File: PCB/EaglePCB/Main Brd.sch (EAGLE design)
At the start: 57 parts, among them J1 1909763-1, J3 1909763-1, U1 ATWINC1500-MR210PB1952-T, U3 MSP430FR2355TDBTRDBT0038A_M, U6 ARJM11C7-114-BA-EW2

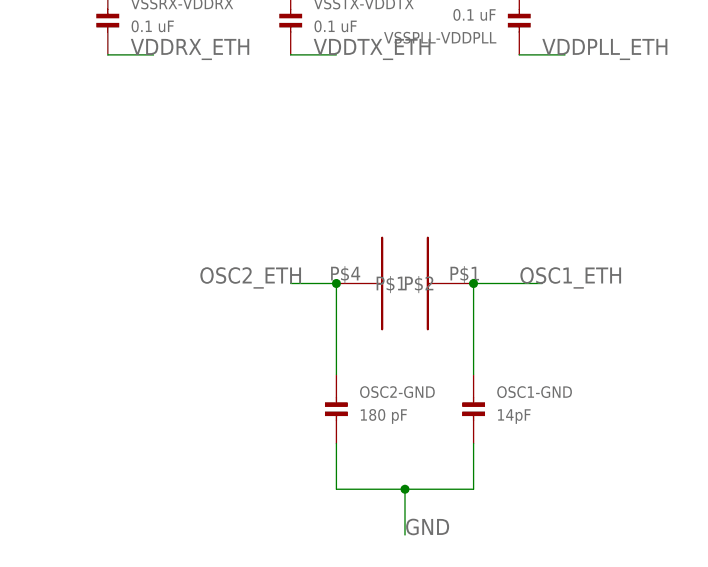
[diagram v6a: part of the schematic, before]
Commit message: new oscillator added into circuit
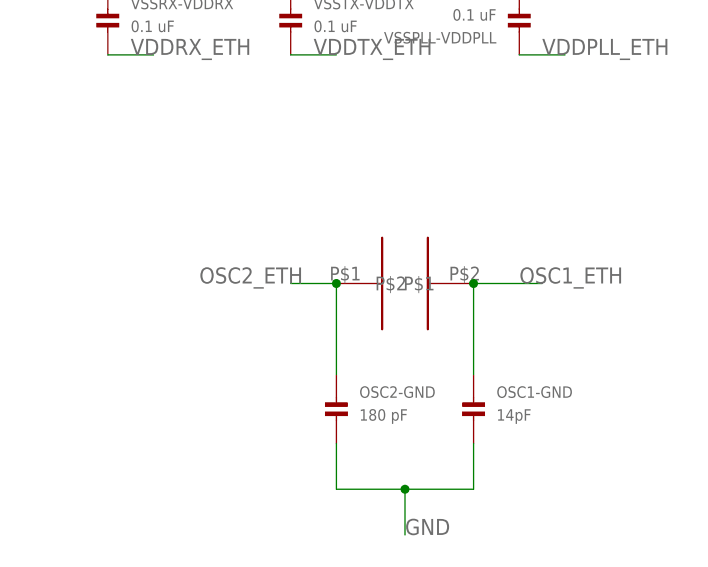
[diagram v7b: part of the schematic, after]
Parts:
- U$2: value CRYSTAL -> J49SMH-P-G-G-K-25M0; device 473:CRYSTAL -> 473:J49SMH-P-G-G-K-25M0
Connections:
- net OSC1_ETH: now also U$2.P$2; no longer U$2.P$1
- net OSC2_ETH: now also U$2.P$1; no longer U$2.P$2
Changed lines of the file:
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@@
 <grid distance="0.1" unitdist="inch" unit="inch" style="lines" multiple="1" display="no" altdistance="0.01" altunitdist="inch" altunit="inch"/>
 <layers>
-<layer number="1" name="Top" color="4" fill="1" visible="no" active="no"/>
-<layer number="16" name="Bottom" color="1" fill="1" visible="no" active="no"/>
-<layer number="17" name="Pads" color="2" fill="1" visible="no" active="no"/>
-<layer number="18" name="Vias" color="2" fill="1" visible="no" active="no"/>
-<layer number="19" name="Unrouted" color="6" fill="1" visible="no" active="no"/>
-<layer number="20" name="Dimension" color="24" fill="1" visible="no" active="no"/>
-<layer number="21" name="tPlace" color="7" fill="1" visible="no" active="no"/>
-<layer number="22" name="bPlace" color="7" fill="1" visible="no" active="no"/>
-<layer number="23" name="tOrigins" color="15" fill="1" visible="no" active="no"/>
-<layer number="24" name="bOrigins" color="15" fill="1" visible="no" active="no"/>
-<layer number="25" name="tNames" color="7" fill="1" visible="no" active="no"/>
-<layer number="26" name="bNames" color="7" fill="1" visible="no" active="no"/>
-<layer number="27" name="tValues" color="7" fill="1" visible="no" active="no"/>
-<layer number="28" name="bValues" color="7" fill="1" visible="no" active="no"/>
+<layer number="1" name="Top" color="4" fill="1" visible="yes" active="no"/>
+<layer number="16" name="Bottom" color="1" fill="1" visible="yes" active="no"/>
+<layer number="17" name="Pads" color="2" fill="1" visible="yes" active="no"/>
+<layer number="18" name="Vias" color="2" fill="1" visible="yes" active="no"/>
+<layer number="19" name="Unrouted" color="6" fill="1" visible="yes" active="no"/>
+<layer number="20" name="Dimension" color="24" fill="1" visible="yes" active="no"/>
+<layer number="21" name="tPlace" color="7" fill="1" visible="yes" active="no"/>
+<layer number="22" name="bPlace" color="7" fill="1" visible="yes" active="no"/>
+<layer number="23" name="tOrigins" color="15" fill="1" visible="yes" active="no"/>
+<layer number="24" name="bOrigins" color="15" fill="1" visible="yes" active="no"/>
+<layer number="25" name="tNames" color="7" fill="1" visible="yes" active="no"/>
+<layer number="26" name="bNames" color="7" fill="1" visible="yes" active="no"/>
+<layer number="27" name="tValues" color="7" fill="1" visible="yes" active="no"/>
+<layer number="28" name="bValues" color="7" fill="1" visible="yes" active="no"/>
 <layer number="29" name="tStop" color="7" fill="3" visible="no" active="no"/>
 <layer number="30" name="bStop" color="7" fill="6" visible="no" active="no"/>
@@
 <layer number="35" name="tGlue" color="7" fill="4" visible="no" active="no"/>
 <layer number="36" name="bGlue" color="7" fill="5" visible="no" active="no"/>
-<layer number="37" name="tTest" color="7" fill="1" visible="no" active="no"/>
-<layer number="38" name="bTest" color="7" fill="1" visible="no" active="no"/>
+<layer number="37" name="tTest" color="7" fill="1" visible="yes" active="no"/>
+<layer number="38" name="bTest" color="7" fill="1" visible="yes" active="no"/>
 <layer number="39" name="tKeepout" color="4" fill="11" visible="no" active="no"/>
 <layer number="40" name="bKeepout" color="1" fill="11" visible="no" active="no"/>
@@
 <layer number="44" name="Drills" color="7" fill="1" visible="no" active="no"/>
 <layer number="45" name="Holes" color="7" fill="1" visible="no" active="no"/>
-<layer number="46" name="Milling" color="3" fill="1" visible="no" active="no"/>
-<layer number="47" name="Measures" color="7" fill="1" visible="no" active="no"/>
-<layer number="48" name="Document" color="7" fill="1" visible="no" active="no"/>
-<layer number="49" name="Reference" color="7" fill="1" visible="no" active="no"/>
-<layer number="50" name="dxf" color="7" fill="1" visible="no" active="no"/>
-<layer number="51" name="tDocu" color="7" fill="1" visible="no" active="no"/>
-<layer number="52" name="bDocu" color="7" fill="1" visible="no" active="no"/>
-<layer number="53" name="tGND_GNDA" color="7" fill="9" visible="no" active="no"/>
-<layer number="54" name="bGND_GNDA" color="1" fill="9" visible="no" active="no"/>
-<layer number="56" name="wert" color="7" fill="1" visible="no" active="no"/>
-<layer number="57" name="tCAD" color="7" fill="1" visible="no" active="no"/>
-<layer number="59" name="tCarbon" color="7" fill="1" visible="no" active="no"/>
-<layer number="60" name="bCarbon" color="7" fill="1" visible="no" active="no"/>
+<layer number="46" name="Milling" color="3" fill="1" visible="yes" active="no"/>
+<layer number="47" name="Measures" color="7" fill="1" visible="yes" active="no"/>
+<layer number="48" name="Document" color="7" fill="1" visible="yes" active="no"/>
+<layer number="49" name="Reference" color="7" fill="1" visible="yes" active="no"/>
+<layer number="50" name="dxf" color="7" fill="1" visible="yes" active="no"/>
+<layer number="51" name="tDocu" color="7" fill="1" visible="yes" active="no"/>
+<layer number="52" name="bDocu" color="7" fill="1" visible="yes" active="no"/>
+<layer number="53" name="tGND_GNDA" color="7" fill="9" visible="yes" active="no"/>
+<layer number="54" name="bGND_GNDA" color="1" fill="9" visible="yes" active="no"/>
+<layer number="56" name="wert" color="7" fill="1" visible="yes" active="no"/>
+<layer number="57" name="tCAD" color="7" fill="1" visible="yes" active="no"/>
+<layer number="59" name="tCarbon" color="7" fill="1" visible="yes" active="no"/>
+<layer number="60" name="bCarbon" color="7" fill="1" visible="yes" active="no"/>
 <layer number="88" name="SimResults" color="9" fill="1" visible="yes" active="yes"/>
 <layer number="89" name="SimProbes" color="9" fill="1" visible="yes" active="yes"/>
@@
 <part name="VSSOSC-VDDOSC" library="microbuilder" deviceset="CAP_CERAMIC" device="0603" value="0.1 uF"/>
 <part name="VSSPLL-VDDPLL" library="microbuilder" deviceset="CAP_CERAMIC" device="0603" value="0.1 uF"/>
-<part name="U$2" library="473" deviceset="CRYSTAL" device=""/>
 <part name="OSC2-GND" library="microbuilder" deviceset="CAP_CERAMIC" device="0603" value="180 pF"/>
 <part name="OSC1-GND" library="microbuilder" deviceset="CAP_CERAMIC" device="0603" value="14pF"/>
+<part name="U$2" library="473" deviceset="J49SMH-P-G-G-K-25M0" device=""/>
 </parts>
 <sheets>
@@
 <attribute name="VALUE" x="363.22" y="27.94" size="1.27" layer="96" font="vector" rot="R180"/>
 </instance>
-<instance part="U$2" gate="G$1" x="353.06" y="-2.54" smashed="yes" rot="R180" grouprefs="ETH_OSC_CIRCUIT"/>
 <instance part="OSC2-GND" gate="G$1" x="345.44" y="-17.78" smashed="yes" grouprefs="ETH_OSC_CIRCUIT">
 <attribute name="NAME" x="347.98" y="-15.24" size="1.27" layer="95" font="vector"/>
@@
 <attribute name="VALUE" x="363.22" y="-17.78" size="1.27" layer="96" font="vector"/>
 </instance>
+<instance part="U$2" gate="G$1" x="353.06" y="-2.54" smashed="yes"/>
 </instances>
 <busses>
@@
 </segment>
 <segment>
-<pinref part="U$2" gate="G$1" pin="P$1"/>
 <wire x1="360.68" y1="-2.54" x2="368.3" y2="-2.54" width="0.1524" layer="91" grouprefs="ETH_OSC_CIRCUIT"/>
 <label x="365.76" y="-2.54" size="1.778" layer="95" grouprefs="ETH_OSC_CIRCUIT"/>
 <wire x1="360.68" y1="-2.54" x2="360.68" y2="-12.7" width="0.1524" layer="91" grouprefs="ETH_OSC_CIRCUIT"/>
-<junction x="360.68" y="-2.54" grouprefs="ETH_OSC_CIRCUIT"/>
 <pinref part="OSC1-GND" gate="G$1" pin="P$1"/>
+<pinref part="U$2" gate="G$1" pin="P$2"/>
+<junction x="360.68" y="-2.54"/>
 </segment>
 </net>
@@
 </segment>
 <segment>
-<pinref part="U$2" gate="G$1" pin="P$2"/>
 <wire x1="345.44" y1="-2.54" x2="340.36" y2="-2.54" width="0.1524" layer="91" grouprefs="ETH_OSC_CIRCUIT"/>
 <label x="330.2" y="-2.54" size="1.778" layer="95" grouprefs="ETH_OSC_CIRCUIT"/>
 <wire x1="345.44" y1="-2.54" x2="345.44" y2="-12.7" width="0.1524" layer="91" grouprefs="ETH_OSC_CIRCUIT"/>
-<junction x="345.44" y="-2.54" grouprefs="ETH_OSC_CIRCUIT"/>
 <pinref part="OSC2-GND" gate="G$1" pin="P$1"/>
-</segment>
-</net>
+<pinref part="U$2" gate="G$1" pin="P$1"/>
+<junction x="345.44" y="-2.54"/>
+</segment>
+</net>

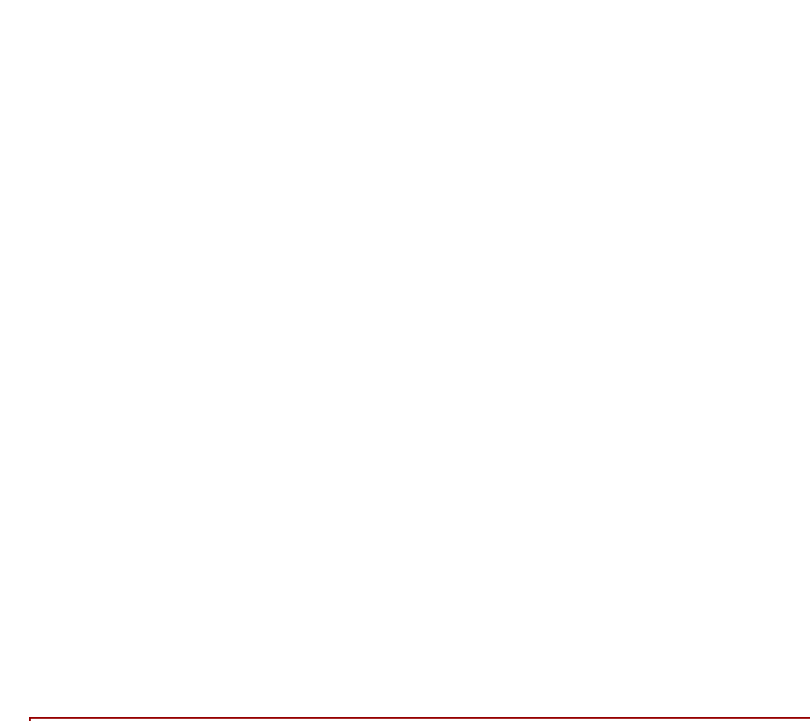
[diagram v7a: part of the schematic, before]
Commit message: added JTAG Port
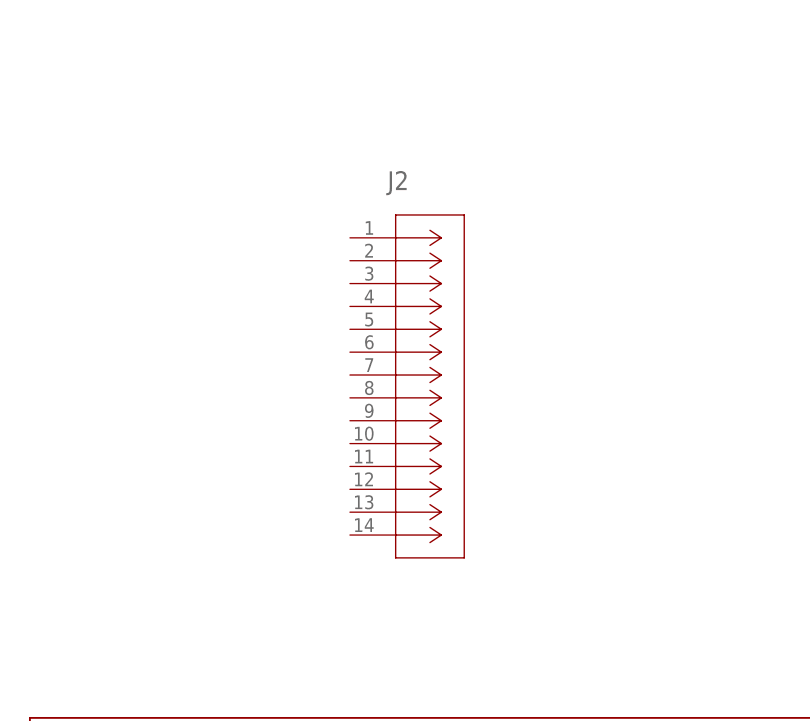
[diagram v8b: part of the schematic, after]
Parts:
- added J2: 702461401, 473:702461401
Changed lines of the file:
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@@
 <grid distance="0.1" unitdist="inch" unit="inch" style="lines" multiple="1" display="no" altdistance="0.01" altunitdist="inch" altunit="inch"/>
 <layers>
-<layer number="1" name="Top" color="4" fill="1" visible="yes" active="no"/>
-<layer number="16" name="Bottom" color="1" fill="1" visible="yes" active="no"/>
-<layer number="17" name="Pads" color="2" fill="1" visible="yes" active="no"/>
-<layer number="18" name="Vias" color="2" fill="1" visible="yes" active="no"/>
-<layer number="19" name="Unrouted" color="6" fill="1" visible="yes" active="no"/>
-<layer number="20" name="Dimension" color="24" fill="1" visible="yes" active="no"/>
-<layer number="21" name="tPlace" color="7" fill="1" visible="yes" active="no"/>
-<layer number="22" name="bPlace" color="7" fill="1" visible="yes" active="no"/>
-<layer number="23" name="tOrigins" color="15" fill="1" visible="yes" active="no"/>
-<layer number="24" name="bOrigins" color="15" fill="1" visible="yes" active="no"/>
-<layer number="25" name="tNames" color="7" fill="1" visible="yes" active="no"/>
-<layer number="26" name="bNames" color="7" fill="1" visible="yes" active="no"/>
-<layer number="27" name="tValues" color="7" fill="1" visible="yes" active="no"/>
-<layer number="28" name="bValues" color="7" fill="1" visible="yes" active="no"/>
+<layer number="1" name="Top" color="4" fill="1" visible="no" active="no"/>
+<layer number="16" name="Bottom" color="1" fill="1" visible="no" active="no"/>
+<layer number="17" name="Pads" color="2" fill="1" visible="no" active="no"/>
+<layer number="18" name="Vias" color="2" fill="1" visible="no" active="no"/>
+<layer number="19" name="Unrouted" color="6" fill="1" visible="no" active="no"/>
+<layer number="20" name="Dimension" color="24" fill="1" visible="no" active="no"/>
+<layer number="21" name="tPlace" color="7" fill="1" visible="no" active="no"/>
+<layer number="22" name="bPlace" color="7" fill="1" visible="no" active="no"/>
+<layer number="23" name="tOrigins" color="15" fill="1" visible="no" active="no"/>
+<layer number="24" name="bOrigins" color="15" fill="1" visible="no" active="no"/>
+<layer number="25" name="tNames" color="7" fill="1" visible="no" active="no"/>
+<layer number="26" name="bNames" color="7" fill="1" visible="no" active="no"/>
+<layer number="27" name="tValues" color="7" fill="1" visible="no" active="no"/>
+<layer number="28" name="bValues" color="7" fill="1" visible="no" active="no"/>
 <layer number="29" name="tStop" color="7" fill="3" visible="no" active="no"/>
 <layer number="30" name="bStop" color="7" fill="6" visible="no" active="no"/>
@@
 <layer number="35" name="tGlue" color="7" fill="4" visible="no" active="no"/>
 <layer number="36" name="bGlue" color="7" fill="5" visible="no" active="no"/>
-<layer number="37" name="tTest" color="7" fill="1" visible="yes" active="no"/>
-<layer number="38" name="bTest" color="7" fill="1" visible="yes" active="no"/>
+<layer number="37" name="tTest" color="7" fill="1" visible="no" active="no"/>
+<layer number="38" name="bTest" color="7" fill="1" visible="no" active="no"/>
 <layer number="39" name="tKeepout" color="4" fill="11" visible="no" active="no"/>
 <layer number="40" name="bKeepout" color="1" fill="11" visible="no" active="no"/>
@@
 <layer number="44" name="Drills" color="7" fill="1" visible="no" active="no"/>
 <layer number="45" name="Holes" color="7" fill="1" visible="no" active="no"/>
-<layer number="46" name="Milling" color="3" fill="1" visible="yes" active="no"/>
-<layer number="47" name="Measures" color="7" fill="1" visible="yes" active="no"/>
-<layer number="48" name="Document" color="7" fill="1" visible="yes" active="no"/>
-<layer number="49" name="Reference" color="7" fill="1" visible="yes" active="no"/>
-<layer number="50" name="dxf" color="7" fill="1" visible="yes" active="no"/>
-<layer number="51" name="tDocu" color="7" fill="1" visible="yes" active="no"/>
-<layer number="52" name="bDocu" color="7" fill="1" visible="yes" active="no"/>
-<layer number="53" name="tGND_GNDA" color="7" fill="9" visible="yes" active="no"/>
-<layer number="54" name="bGND_GNDA" color="1" fill="9" visible="yes" active="no"/>
-<layer number="56" name="wert" color="7" fill="1" visible="yes" active="no"/>
-<layer number="57" name="tCAD" color="7" fill="1" visible="yes" active="no"/>
-<layer number="59" name="tCarbon" color="7" fill="1" visible="yes" active="no"/>
-<layer number="60" name="bCarbon" color="7" fill="1" visible="yes" active="no"/>
+<layer number="46" name="Milling" color="3" fill="1" visible="no" active="no"/>
+<layer number="47" name="Measures" color="7" fill="1" visible="no" active="no"/>
+<layer number="48" name="Document" color="7" fill="1" visible="no" active="no"/>
+<layer number="49" name="Reference" color="7" fill="1" visible="no" active="no"/>
+<layer number="50" name="dxf" color="7" fill="1" visible="no" active="no"/>
+<layer number="51" name="tDocu" color="7" fill="1" visible="no" active="no"/>
+<layer number="52" name="bDocu" color="7" fill="1" visible="no" active="no"/>
+<layer number="53" name="tGND_GNDA" color="7" fill="9" visible="no" active="no"/>
+<layer number="54" name="bGND_GNDA" color="1" fill="9" visible="no" active="no"/>
+<layer number="56" name="wert" color="7" fill="1" visible="no" active="no"/>
+<layer number="57" name="tCAD" color="7" fill="1" visible="no" active="no"/>
+<layer number="59" name="tCarbon" color="7" fill="1" visible="no" active="no"/>
+<layer number="60" name="bCarbon" color="7" fill="1" visible="no" active="no"/>
 <layer number="88" name="SimResults" color="9" fill="1" visible="yes" active="yes"/>
 <layer number="89" name="SimProbes" color="9" fill="1" visible="yes" active="yes"/>
@@
 <part name="OSC1-GND" library="microbuilder" deviceset="CAP_CERAMIC" device="0603" value="14pF"/>
 <part name="U$2" library="473" deviceset="J49SMH-P-G-G-K-25M0" device=""/>
+<part name="J2" library="473" deviceset="702461401" device=""/>
 </parts>
 <sheets>
@@
 </instance>
 <instance part="U$2" gate="G$1" x="353.06" y="-2.54" smashed="yes"/>
+<instance part="J2" gate="A" x="76.2" y="27.94" smashed="yes">
+<attribute name="NAME" x="80.3656" y="33.2486" size="2.0828" layer="95" ratio="6" rot="SR0"/>
+</instance>
 </instances>
 <busses>
